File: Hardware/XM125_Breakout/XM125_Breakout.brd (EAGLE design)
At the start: 160 x 100 mm, 2 parts

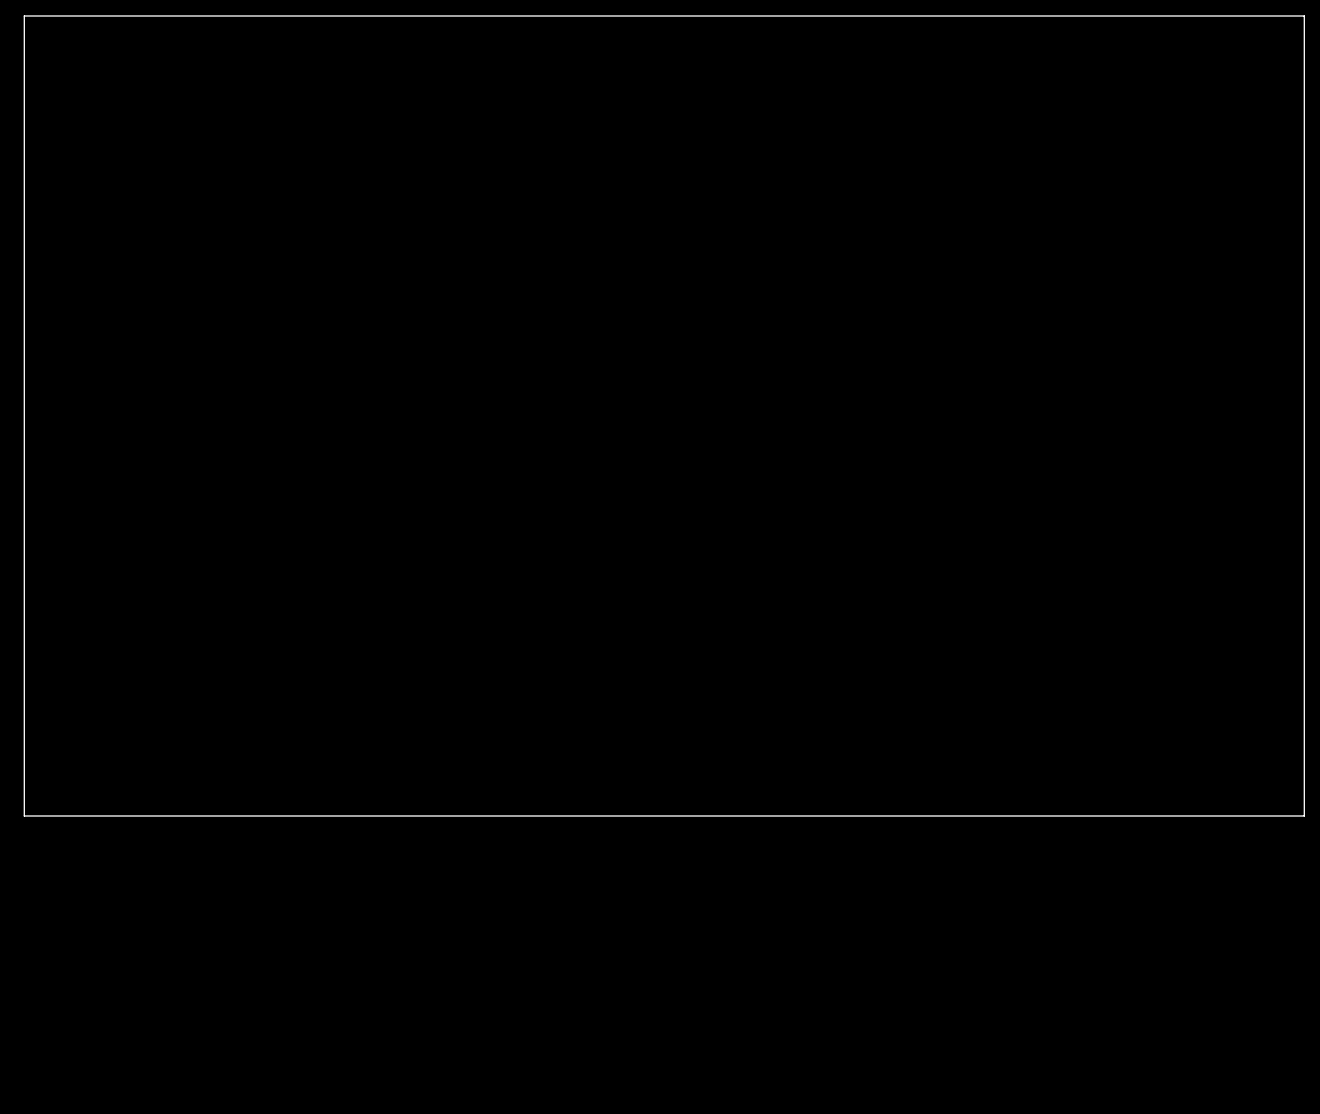
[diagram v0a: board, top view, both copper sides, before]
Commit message: Removed uneeded board files; updates to breakout board
Removed the 1x1 and Thing+ board options; updated the schematic and layout - grouped together the needed sections in the layout
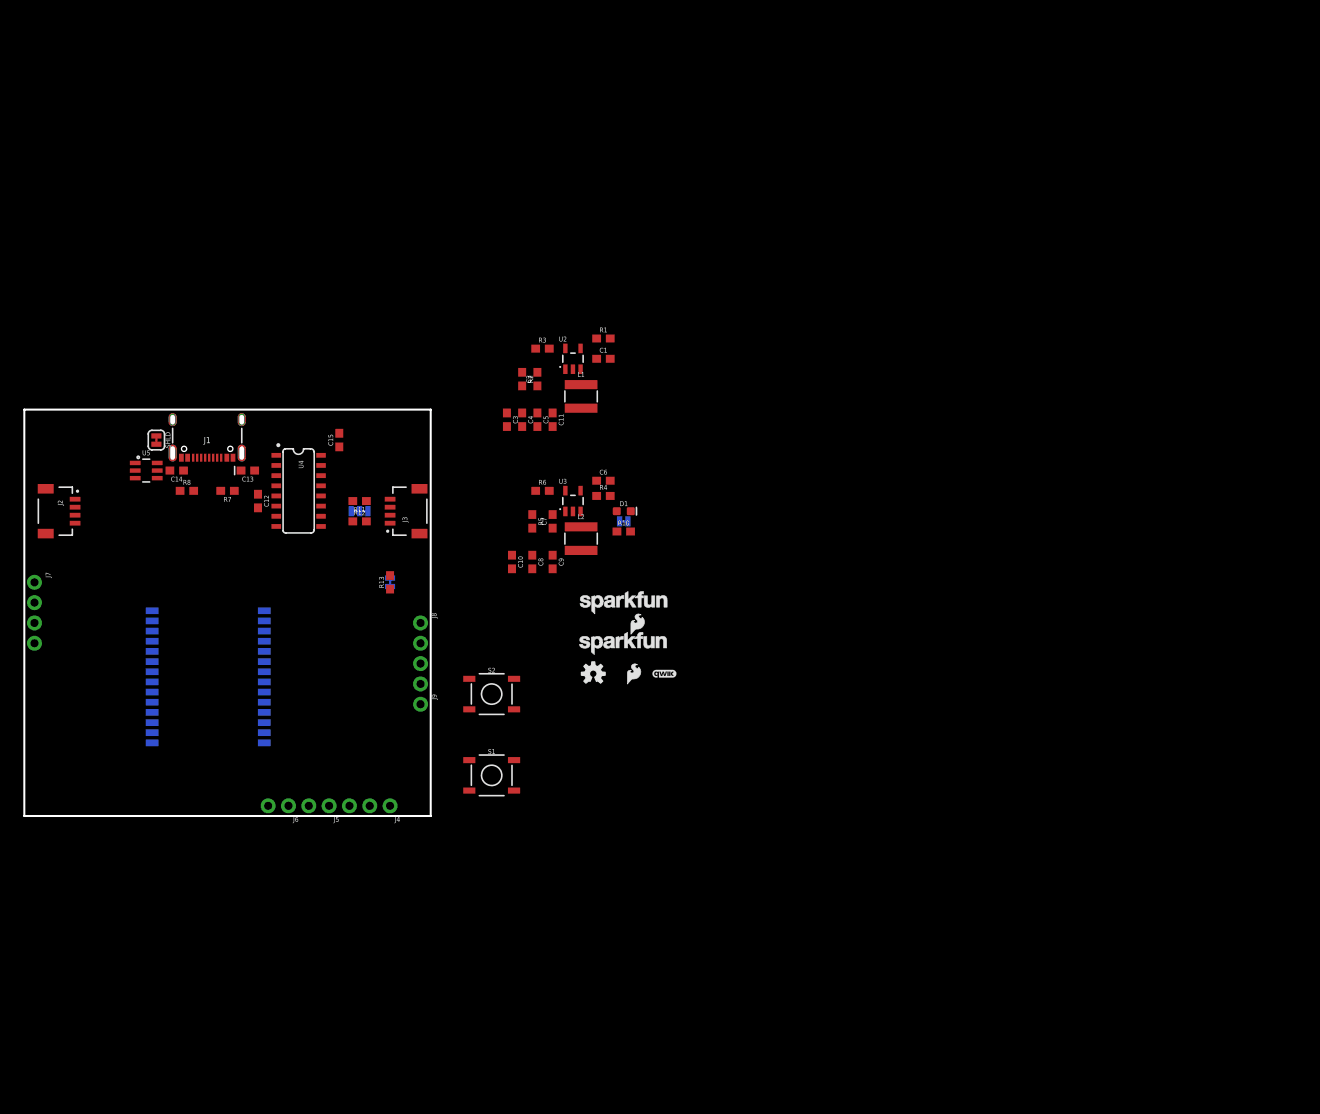
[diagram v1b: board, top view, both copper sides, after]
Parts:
- removed FRAME1: FRAME-LEDGER, SparkFun-Aesthetics:CREATIVE_COMMONS
- added 3V3, JP2, SHLD: JUMPER-SMT_2_NC_TRACE_SILK, SparkFun-Jumpers:SMT-JUMPER_2_NC_TRACE_SILK
- added C1, C11, C2, C3, C6, C8: 22uF, SparkFun-Capacitors:0603
- added C10, C5: 1.0uF, SparkFun-Capacitors:0603
- added C12: 10nF, SparkFun-Capacitors:0603
- added C13: 10uF, SparkFun-Capacitors:0603-POLAR
- added C14, C15, C4, C9: 0.1uF, SparkFun-Capacitors:0603
- added C7: 22pF, SparkFun-Capacitors:0603
- added D1: Red, SparkFun-LED:LED-0603
- added FRAME2: FRAME-LETTER, SparkFun-Aesthetics:CREATIVE_COMMONS
- added I2C: JUMPER-SMT_3_2-NC_TRACE_SILK, SparkFun-Jumpers:SMT-JUMPER_3_2-NC_TRACE_SILK
- added J1: (no value), SparkFun-Connectors:USB-C-16P-2LAYER-PADS
- added J2, J3: QWIIC_RIGHT_ANGLE, SparkFun-Connectors:JST04_1MM_RA
- added J4: (no value), SparkFun-Connectors:1X03_NO_SILK
- added J5, J6: (no value), SparkFun-Connectors:1X02_NO_SILK
- added J7, J8: (no value), SparkFun-Connectors:1X04_NO_SILK
- added J9: (no value), SparkFun-Connectors:1X01_NO_SILK_STAND
- added L1, L2: 2.2μH, SparkFun-Coils:INDUCTOR_4X4MM
- added LOGO2: QWIIC_LOGO_3MM, SparkFun-Aesthetics:QWIIC_3MM
- added LOGO3: SFE_LOGO_NAME_FLAME.1_INCH, SparkFun-Aesthetics:SFE_LOGO_NAME_FLAME_.1
- added LOGO4: OSHW-LOGOS, SparkFun-Aesthetics:OSHW-LOGO-S
- added LOGO5: SFE_LOGO_FLAME.1_INCH, SparkFun-Aesthetics:SFE_LOGO_FLAME_.1
- added LOGO6: SFE_LOGO_NAME.1_INCH, SparkFun-Aesthetics:SFE_LOGO_NAME_.1
- added R1, R4, R6: 100k, SparkFun-Resistors:0603
- added R10: 1k, SparkFun-Resistors:0603
- added R11, R12: 2.2k, SparkFun-Resistors:0603
- added R13: 10k, SparkFun-Resistors:0603
- added R2: 300k, SparkFun-Resistors:0603
- added R3: 150k, SparkFun-Resistors:0603
- added R5: 453k, SparkFun-Resistors:0603
- added R7, R8: 5.1k, SparkFun-Resistors:0603
- added S1, S2: (no value), SparkFun-Switches:TACTILE_SWITCH_SMD_5.2MM
- added U1: XM125, XM125:XM125_ACC
- added U2, U3: (no value), SparkFun-IC-Power:SOT23-5
- added U4: CH340C, SparkFun-IC-Comms:SO016
- added U5: ESD Diode, SparkFun-DiscreteSemi:SOT-23-6
- moved LOGO1 161.4 mm to (143.5, 64.8)
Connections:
- new net 1.8V: C11.1, C2.1, C3.1, C4.1, C5.1, J7.4, L1.P$2, R2.2, U1.3
- new net 3.3V: 3V3.2, C10.1, C15.1, C7.1, C8.1, C9.1, I2C.2, J2.2, J3.2, J7.3, JP2.2, L2.P$2, R5.2, S2.3, S2.4, U1.1, U4.16
- new net CH340-CTS: U1.8, U4.9
- new net CH340-RTS: U1.9, U4.14
- new net CH340-RX: U1.5, U4.3
- new net CH340-TX: U1.6, U4.2
- new net DEBUG_UART-RX: J5.1, U1.21
- new net DEBUG_UART-TX: J5.2, U1.23
- new net GND: C1.2, C10.2, C11.2, C12.2, C13.-, C14.2, C15.2, C3.2, C4.2, C5.2, C6.2, C8.2, C9.2, D1.C, J1.GND, J1.GND2, J2.1, J3.1, J7.1, J7.2, R11.1, R12.1, R3.2, R6.1, R7.1, R8.1, SHLD.1, U1.10, U1.13, U1.16, U1.19, U1.2, U1.22, U1.27, U1.4, U1.7, U2.2, U3.2, U4.1, U5.2
- new net INT: J4.1
- new net N$1: J1.A6, J1.B6, U4.5, U5.4
- new net N$10: J1.B5, R8.2
- new net N$11: J1.A5, R7.2
- new net N$12: C12.1, U4.4
- new net N$14: 3V3.1, R10.2
- new net N$15: D1.A, R10.1
- new net N$16: I2C.3, R11.2
- new net N$17: I2C.1, R12.2
- new net N$18: JP2.1, R13.2
- new net N$19: S1.3, S1.4
- new net N$2: J1.A7, J1.B7, U4.6, U5.6
- new net N$3: L1.P$1, U2.3
- new net N$4: R1.2, U2.1
- new net N$5: R4.2, U3.1
- new net N$6: C2.2, R2.1, R3.1, U2.5
- new net N$7: L2.P$1, U3.3
- new net N$8: C7.2, R5.1, R6.2, U3.5
- new net N$9: J1.SHLD1, J1.SHLD2, J1.SHLD3, J1.SHLD4, SHLD.2
- new net SCL: J2.4, J3.4, J4.3, U1.17
- new net SDA: J2.3, J3.3, J4.2, U1.18
- new net SWD_CLK: J6.2, U1.12
- new net SWD_IO: J6.1, U1.11
- new net V_USB: C1.1, C13.+, C14.1, C6.1, J1.VBUS1, J1.VBUS2, R1.1, R4.1, U2.4, U3.4, U5.5
- new net WAKE_UP: U1.15
- new net XM125_GPIO0: J8.1, U1.24
- new net XM125_GPIO1: J8.2, U1.25
- new net XM125_GPIO2/BOOT0: J8.3, S2.1, S2.2, U1.26
- new net XM125_INT: J8.4, R13.1, U1.28
- new net XM125_RESET: J9.1, S1.1, S1.2, U1.14
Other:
- board size 160 x 100 mm -> 50.8 x 50.8 mm
- board text added: "M. Chodikov"

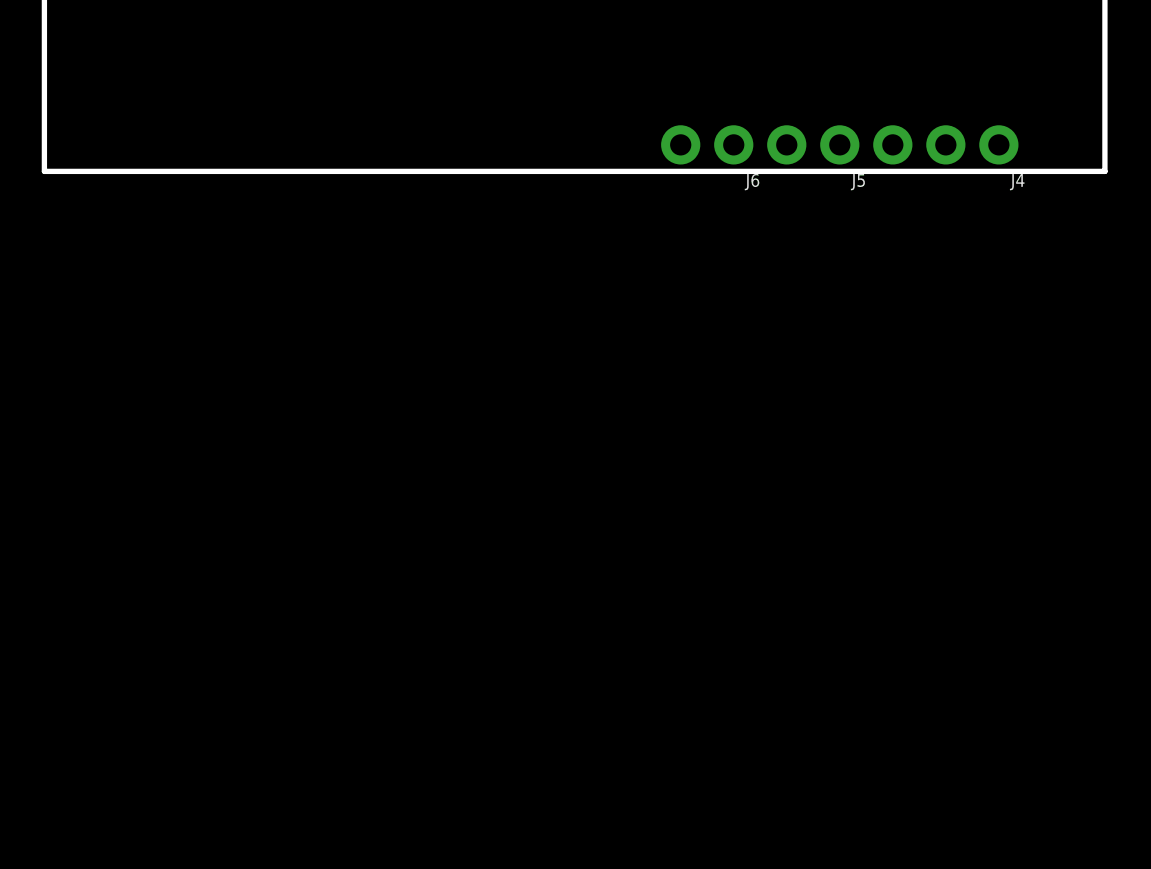
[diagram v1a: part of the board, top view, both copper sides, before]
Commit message: Addition of further documentation; initial schematic ready for review
Fixed small issues on schematic; added I2C documentation to the repo
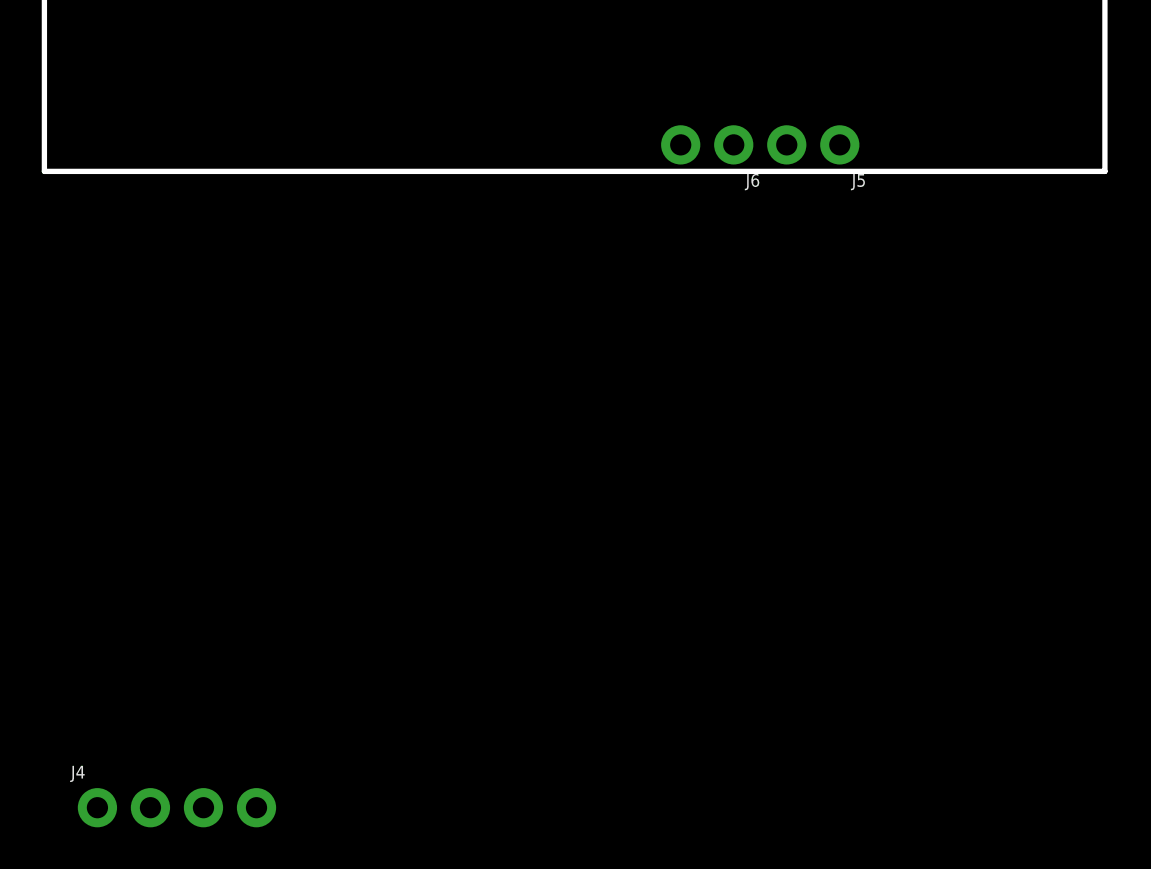
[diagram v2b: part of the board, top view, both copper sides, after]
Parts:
- J4: device SparkFun-Connectors:1X03_NO_SILK -> SparkFun-Connectors:1X04_NO_SILK
- moved J4 53.6 mm to (2.54, -30.5), turned to 0 degrees
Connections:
- removed net N$19: S1.3, S1.4
- new net XM125_I2C_ADDRESS: J4.4, U1.20
- net 3.3V: now also S1.3, S1.4
- net WAKE_UP: now also S2.1, S2.2
- net XM125_GPIO2/BOOT0: no longer S2.1, S2.2
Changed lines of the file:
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@@
 <attribute name="VALUE" x="49.022" y="36.449" size="0.6096" layer="27" font="vector" ratio="20" rot="R90"/>
-</element>
-<element name="J4" library="SparkFun-Connectors" package="1X03_NO_SILK" value="" x="45.72" y="1.27" smashed="yes" rot="R180">
-<attribute name="NAME" x="46.99" y="-0.127" size="0.6096" layer="25" font="vector" ratio="20" rot="R180"/>
-<attribute name="VALUE" x="46.99" y="3.302" size="0.6096" layer="27" font="vector" ratio="20" rot="R180"/>
 </element>
 <element name="J5" library="SparkFun-Connectors" package="1X02_NO_SILK" value="" x="38.1" y="1.27" smashed="yes" rot="R180">
@@
 <element name="LOGO5" library="SparkFun-Aesthetics" package="SFE_LOGO_FLAME_.1" value="SFE_LOGO_FLAME.1_INCH" x="76.2" y="17.78" smashed="yes"/>
 <element name="LOGO6" library="SparkFun-Aesthetics" package="SFE_LOGO_NAME_.1" value="SFE_LOGO_NAME.1_INCH" x="74.93" y="26.67" smashed="yes"/>
+<element name="J4" library="SparkFun-Connectors" package="1X04_NO_SILK" value="" x="2.54" y="-30.48" smashed="yes">
+<attribute name="NAME" x="1.27" y="-29.083" size="0.6096" layer="25" font="vector" ratio="20"/>
+<attribute name="PROD_ID" value="CONN-09696" x="2.54" y="-30.48" size="1.778" layer="27" font="vector" ratio="15" display="off"/>
+<attribute name="VALUE" x="1.27" y="-32.512" size="0.6096" layer="27" font="vector" ratio="20"/>
+</element>
 </elements>
 <signals>
@@
 <contactref element="S2" pad="3"/>
 <contactref element="S2" pad="4"/>
+<contactref element="S1" pad="4"/>
+<contactref element="S1" pad="3"/>
 <wire x1="69.596" y1="33.1978" x2="74.4093" y2="36.83" width="0" layer="19" extent="1-16"/>
 <wire x1="66.04" y1="32.6" x2="69.596" y2="33.1978" width="0" layer="19" extent="1-1"/>
@@
 <wire x1="55.626" y1="13.335" x2="45.72" y2="28.6893" width="0" layer="19" extent="1-16"/>
 <wire x1="61.214" y1="13.335" x2="55.626" y2="13.335" width="0" layer="19" extent="1-1"/>
+<wire x1="61.214" y1="3.175" x2="61.214" y2="13.335" width="0" layer="19" extent="1-1"/>
+<wire x1="55.626" y1="3.175" x2="61.214" y2="3.175" width="0" layer="19" extent="1-1"/>
 <wire x1="6.35" y1="38.6" x2="37.09" y2="45.085" width="0" layer="19" extent="1-1"/>
 <wire x1="1.27" y1="24.13" x2="6.35" y2="38.6" width="0" layer="19" extent="1-1"/>
@@
 <signal name="WAKE_UP">
 <contactref element="U1" pad="15"/>
+<contactref element="S2" pad="1"/>
+<contactref element="S2" pad="2"/>
+<wire x1="55.626" y1="17.145" x2="61.214" y2="17.145" width="0" layer="19" extent="1-1"/>
+<wire x1="29.9974" y1="25.654" x2="55.626" y2="17.145" width="0" layer="19" extent="1-16"/>
 </signal>
 <signal name="SCL">
@@
 <contactref element="J3" pad="4"/>
 <contactref element="J4" pad="3"/>
-<wire x1="29.9974" y1="23.114" x2="45.72" y2="39.6" width="0" layer="19" extent="1-1"/>
-<wire x1="40.64" y1="1.27" x2="29.9974" y2="23.114" width="0" layer="19" extent="1-1"/>
-<wire x1="6.35" y1="36.6" x2="29.9974" y2="23.114" width="0" layer="19" extent="1-1"/>
+<wire x1="29.9974" y1="23.114" x2="45.72" y2="39.6" width="0" layer="19" extent="1-16"/>
+<wire x1="6.35" y1="36.6" x2="29.9974" y2="23.114" width="0" layer="19" extent="1-16"/>
+<wire x1="7.62" y1="-30.48" x2="29.9974" y2="23.114" width="0" layer="19" extent="16-16"/>
 </signal>
 <signal name="SDA">
@@
 <contactref element="J3" pad="3"/>
 <contactref element="J4" pad="2"/>
-<wire x1="29.9974" y1="21.844" x2="45.72" y2="38.6" width="0" layer="19" extent="1-1"/>
-<wire x1="43.18" y1="1.27" x2="29.9974" y2="21.844" width="0" layer="19" extent="1-1"/>
-<wire x1="6.35" y1="37.6" x2="29.9974" y2="21.844" width="0" layer="19" extent="1-1"/>
+<wire x1="29.9974" y1="21.844" x2="45.72" y2="38.6" width="0" layer="19" extent="1-16"/>
+<wire x1="6.35" y1="37.6" x2="29.9974" y2="21.844" width="0" layer="19" extent="1-16"/>
+<wire x1="5.08" y1="-30.48" x2="29.9974" y2="21.844" width="0" layer="19" extent="16-16"/>
 </signal>
 <signal name="XM125_RESET">
@@
 <contactref element="U1" pad="26"/>
 <contactref element="J8" pad="3"/>
-<contactref element="S2" pad="1"/>
-<contactref element="S2" pad="2"/>
-<wire x1="55.626" y1="17.145" x2="61.214" y2="17.145" width="0" layer="19" extent="1-1"/>
-<wire x1="49.53" y1="19.05" x2="55.626" y2="17.145" width="0" layer="19" extent="1-1"/>
-<wire x1="29.9974" y1="11.684" x2="49.53" y2="19.05" width="0" layer="19" extent="1-1"/>
+<wire x1="29.9974" y1="11.684" x2="49.53" y2="19.05" width="0" layer="19" extent="16-16"/>
 </signal>
 <signal name="XM125_GPIO1">
@@
 <wire x1="45.72" y1="29.7307" x2="45.72" y2="30.06" width="0" layer="19" extent="1-1"/>
 </signal>
-<signal name="INT">
-<contactref element="J4" pad="1"/>
-</signal>
 <signal name="N$12">
 <contactref element="C12" pad="1"/>
@@
 <wire x1="29.21" y1="40.22" x2="31.49" y2="41.275" width="0" layer="19" extent="1-1"/>
 </signal>
-<signal name="N$19">
-<contactref element="S1" pad="4"/>
-<contactref element="S1" pad="3"/>
-<wire x1="55.626" y1="3.175" x2="61.214" y2="3.175" width="0" layer="19" extent="1-1"/>
+<signal name="XM125_I2C_ADDRESS">
+<contactref element="U1" pad="20"/>
+<contactref element="J4" pad="4"/>
+<wire x1="10.16" y1="-30.48" x2="29.9974" y2="19.304" width="0" layer="19" extent="16-16"/>
+</signal>
+<signal name="INT">
+<contactref element="J4" pad="1"/>
 </signal>
 </signals>
